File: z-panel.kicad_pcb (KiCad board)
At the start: 2 copper layers, 80 x 80 mm, 27 parts, among them J1 MOLEX_FFC-14, J2 PC104PTH, J3 PC104PTH, J4 PC104PTH, J5 PC104PTH, J6 SMA, U100 OPA380, U110 OPA380, U120 OPA380, U130 OPA380

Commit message: added 3d model for photodiode
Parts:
- moved D100 4.47 mm to (200.0, 111.0)
- moved D110 3.16 mm to (216.0, 110.0)
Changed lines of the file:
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@@
   (general
     (links 62)
-    (no_connects 22)
+    (no_connects 61)
     (area 109.924999 59.924999 190.075001 140.075001)
     (thickness 1.6)
-    (drawings 4)
+    (drawings 8)
     (tracks 0)
     (zones 0)
@@
   )
   (module SFUSat:SFH2430 (layer F.Cu)
-    (at 204 109)
+    (at 200 111)
     (fp_text reference D100 (at 1.5 3.25) (layer F.SilkS)
       (effects (font (size 1 1) (thickness 0.15)))
@@
     (pad 1 smd rect (at 3.05 0) (size 1.4 2) (layers F.Cu F.Paste F.Mask)
       (net 3 "Net-(C100-Pad2)"))
+    (model ../../../../../home/tobi/Cubesat/z-panel/KiCad-Lib/SFUSat.pretty/SFH_2430.wrl
+      (at (xyz 0 0 0))
+      (scale (xyz 1 1 1))
+      (rotate (xyz 0 0 0))
+    )
   )
   (module SFUSat:SFH2430 (layer F.Cu)
-    (at 213 109)
+    (at 216 110)
     (fp_text reference D110 (at 1.5 3.25) (layer F.SilkS)
       (effects (font (size 1 1) (thickness 0.15)))
@@
     (pad 1 smd rect (at 3.05 0) (size 1.4 2) (layers F.Cu F.Paste F.Mask)
       (net 5 "Net-(C110-Pad2)"))
+    (model ../../../../../home/tobi/Cubesat/z-panel/KiCad-Lib/SFUSat.pretty/SFH_2430.wrl
+      (at (xyz 0 0 0))
+      (scale (xyz 1 1 1))
+      (rotate (xyz 0 0 0))
+    )
   )
   (module SFUSat:SFH2430 (layer F.Cu)
@@
     (pad 1 smd rect (at 3.05 0) (size 1.4 2) (layers F.Cu F.Paste F.Mask)
       (net 7 "Net-(C120-Pad2)"))
+    (model ../../../../../home/tobi/Cubesat/z-panel/KiCad-Lib/SFUSat.pretty/SFH_2430.wrl
+      (at (xyz 0 0 0))
+      (scale (xyz 1 1 1))
+      (rotate (xyz 0 0 0))
+    )
   )
   (module SFUSat:SFH2430 (layer F.Cu)
@@
     (pad 1 smd rect (at 3.05 0) (size 1.4 2) (layers F.Cu F.Paste F.Mask)
       (net 9 "Net-(C130-Pad2)"))
+    (model ../../../../../home/tobi/Cubesat/z-panel/KiCad-Lib/SFUSat.pretty/SFH_2430.wrl
+      (at (xyz 0 0 0))
+      (scale (xyz 1 1 1))
+      (rotate (xyz 0 0 0))
+    )
   )
   (module SFUSat:MOLEX_FFC-14 (layer F.Cu)
@@
   (module SFUSat:VSSOP_8 (layer F.Cu)
     (at 214 73)
-    (fp_text reference U130 (at -0.1 4.1) (layer F.SilkS)
+    (fp_text reference U130 (at 3 -1) (layer F.SilkS)
       (effects (font (size 1 1) (thickness 0.15)))
     )
@@
       (solder_paste_margin_ratio -0.1))
   )
+  (dimension 4 (width 0.3) (layer Dwgs.User)
+    (gr_text "4.000 mm" (at 103.65 62 270) (layer Dwgs.User)
+      (effects (font (size 1.5 1.5) (thickness 0.3)))
+    )
+    (feature1 (pts (xy 114 64) (xy 102.3 64)))
+    (feature2 (pts (xy 114 60) (xy 102.3 60)))
+    (crossbar (pts (xy 105 60) (xy 105 64)))
+    (arrow1a (pts (xy 105 64) (xy 104.413579 62.873496)))
+    (arrow1b (pts (xy 105 64) (xy 105.586421 62.873496)))
+    (arrow2a (pts (xy 105 60) (xy 104.413579 61.126504)))
+    (arrow2b (pts (xy 105 60) (xy 105.586421 61.126504)))
+  )
+  (dimension 4 (width 0.3) (layer Dwgs.User)
+    (gr_text "4.000 mm" (at 112 55.65) (layer Dwgs.User)
+      (effects (font (size 1.5 1.5) (thickness 0.3)))
+    )
+    (feature1 (pts (xy 110 64) (xy 110 54.3)))
+    (feature2 (pts (xy 114 64) (xy 114 54.3)))
+    (crossbar (pts (xy 114 57) (xy 110 57)))
+    (arrow1a (pts (xy 110 57) (xy 111.126504 56.413579)))
+    (arrow1b (pts (xy 110 57) (xy 111.126504 57.586421)))
+    (arrow2a (pts (xy 114 57) (xy 112.873496 56.413579)))
+    (arrow2b (pts (xy 114 57) (xy 112.873496 57.586421)))
+  )
+  (dimension 80 (width 0.3) (layer Dwgs.User)
+    (gr_text "80.000 mm" (at 150 49.65) (layer Dwgs.User)
+      (effects (font (size 1.5 1.5) (thickness 0.3)))
+    )
+    (feature1 (pts (xy 190 60) (xy 190 48.3)))
+    (feature2 (pts (xy 110 60) (xy 110 48.3)))
+    (crossbar (pts (xy 110 51) (xy 190 51)))
+    (arrow1a (pts (xy 190 51) (xy 188.873496 51.586421)))
+    (arrow1b (pts (xy 190 51) (xy 188.873496 50.413579)))
+    (arrow2a (pts (xy 110 51) (xy 111.126504 51.586421)))
+    (arrow2b (pts (xy 110 51) (xy 111.126504 50.413579)))
+  )
+  (dimension 80 (width 0.3) (layer Dwgs.User)
+    (gr_text "80.000 mm" (at 96.65 100 270) (layer Dwgs.User)
+      (effects (font (size 1.5 1.5) (thickness 0.3)))
+    )
+    (feature1 (pts (xy 110 140) (xy 95.3 140)))
+    (feature2 (pts (xy 110 60) (xy 95.3 60)))
+    (crossbar (pts (xy 98 60) (xy 98 140)))
+    (arrow1a (pts (xy 98 140) (xy 97.413579 138.873496)))
+    (arrow1b (pts (xy 98 140) (xy 98.586421 138.873496)))
+    (arrow2a (pts (xy 98 60) (xy 97.413579 61.126504)))
+    (arrow2b (pts (xy 98 60) (xy 98.586421 61.126504)))
+  )
   (gr_line (start 190 60) (end 190 140) (layer Edge.Cuts) (width 0.15))

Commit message: layout complete
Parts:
- added REF**: FFC-Fasteners-8mm, SFUSat:FFC-Fasteners-8mm, F.Cu at (150.0, 134.0)
- moved D130 110.9 mm to (114.2, 125.4), turned to 90 degrees
- moved U130 107.8 mm to (119.8, 125.4), turned to 270 degrees
- moved R130 99.8 mm to (119.8, 120.8), turned to 180 degrees
- moved R131 99.6 mm to (123.8, 126.2), turned to 270 degrees
- moved C130 99.1 mm to (119.8, 122.2), turned to 180 degrees
- moved D100 93.0 mm to (114.2, 75.0), turned to 90 degrees
- moved U100 91.8 mm to (120.0, 75.0), turned to 270 degrees
- moved C100 89.7 mm to (120.0, 72.0), turned to 180 degrees
- moved R100 89.1 mm to (120.0, 70.6), turned to 180 degrees
- moved R101 86.9 mm to (124.0, 75.8), turned to 270 degrees
- moved U120 56.8 mm to (180.4, 125.2), turned to 90 degrees
- moved R121 52.0 mm to (176.4, 124.4), turned to 90 degrees
- moved R120 51.8 mm to (180.4, 129.6)
- moved D120 51.7 mm to (186.2, 125.2), turned to 270 degrees
- moved U110 49.6 mm to (180.0, 75.0), turned to 90 degrees
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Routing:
- net /3V3: track 0.00 -> 171.5 mm, vias 0 -> 6
- net /D2: track 0.00 -> 127.5 mm
- net /D1: track 0.00 -> 79.9 mm
- net /D4: track 0.00 -> 37.0 mm
- net /D3: track 0.00 -> 36.7 mm
- net GND: track 0.00 -> 29.3 mm, vias 0 -> 20
- net Net-(A1-Pad1): track 0.00 -> 29.0 mm
- net Net-(C110-Pad2): track 0.00 -> 10.6 mm
- net Net-(C130-Pad2): track 0.00 -> 10.6 mm
- net Net-(C100-Pad2): track 0.00 -> 10.6 mm
- net Net-(C120-Pad2): track 0.00 -> 10.6 mm
- added copper zone on B.Cu, net GND
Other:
- outline, holes or cut-outs redrawn
- net class Long added: clearance 0.2, trace_width 0.25, via_dia 0.6, via_drill 0.4
- net class RF added: clearance 0.2, trace_width 1.11538, via_dia 0.6, via_drill 0.4

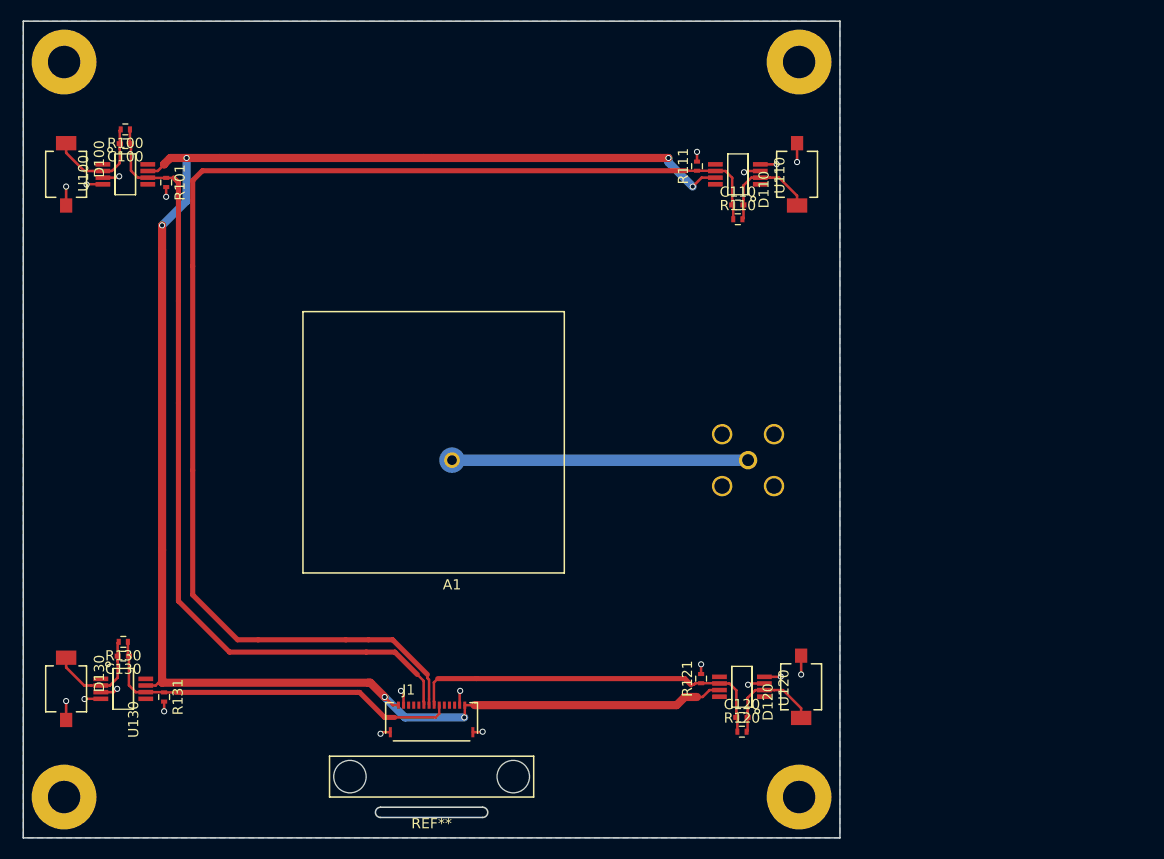
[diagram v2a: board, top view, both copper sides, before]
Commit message: added slots for coax access and adjusted FFC position
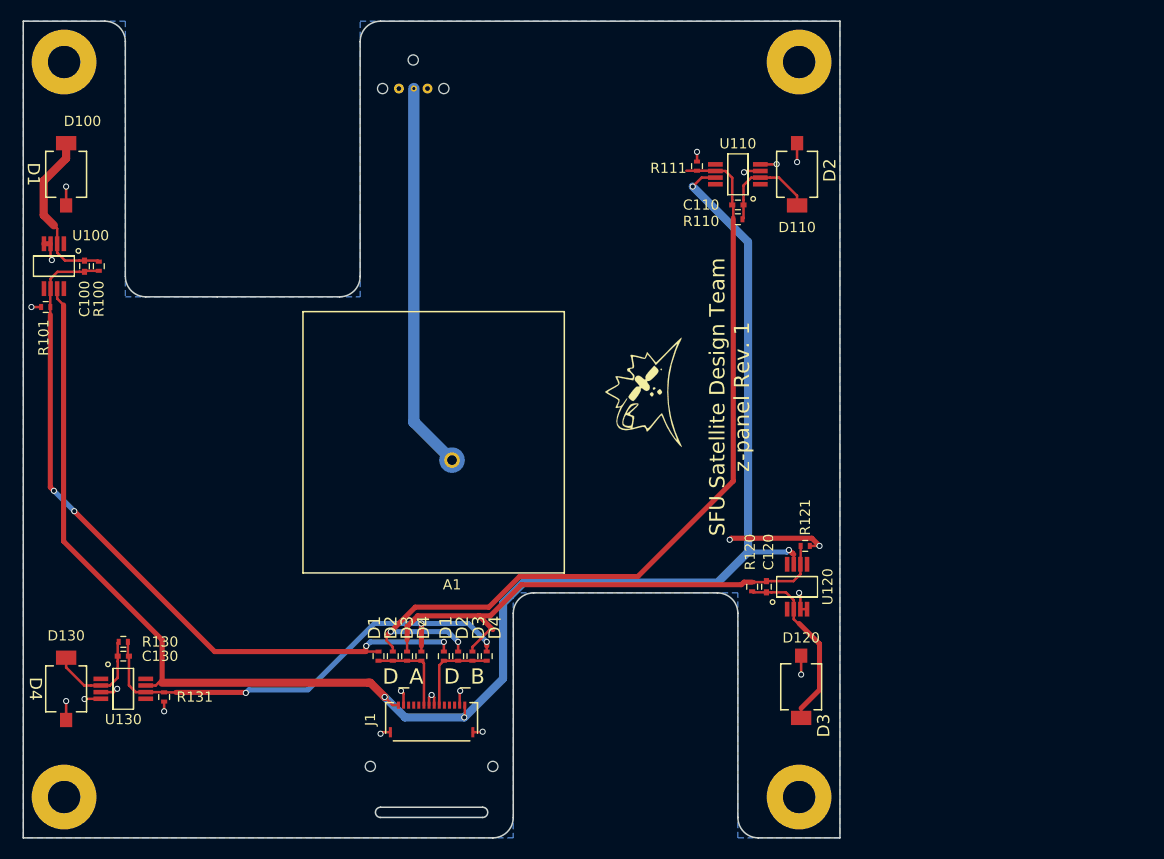
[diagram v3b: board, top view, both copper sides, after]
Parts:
- removed the REF** at (150.0, 134.0)
- added G***: LOGO, SFUSat:SFUSat_15mm_2, F.Cu at (170.8, 96.4)
- added J7: TEST_1P, SFUSat:via-0.97mm, F.Cu at (149.6, 66.6)
- added J8: TEST_1P, SFUSat:via-0.97mm, F.Cu at (146.8, 66.6)
- added R1: 0R, SFUSat-res:R_0402, F.Cu at (144.8, 122.2)
- added R2: 0R, SFUSat-res:R_0402, F.Cu at (151.2, 122.2)
- added R3: 0R, SFUSat-res:R_0402, F.Cu at (146.2, 122.2)
- added R4: 0R, SFUSat-res:R_0402, F.Cu at (152.6, 122.2)
- added R5: 0R, SFUSat-res:R_0402, F.Cu at (147.6, 122.2)
- added R6: 0R, SFUSat-res:R_0402, F.Cu at (154.0, 122.2)
- added R7: 0R, SFUSat-res:R_0402, F.Cu at (149.0, 122.2)
- added R8: 0R, SFUSat-res:R_0402, F.Cu at (155.4, 122.2)
- added REF**: NPTH-1mm, SFUSat:NPTH-1mm, F.Cu at (148.2, 63.8)
- added REF**: NPTH-1mm, SFUSat:NPTH-1mm, F.Cu at (151.2, 66.6)
- added REF**: NPTH-1mm, SFUSat:NPTH-1mm, F.Cu at (156.0, 133.0)
- added REF**: NPTH-1mm, SFUSat:NPTH-1mm, F.Cu at (144.0, 133.0)
- added REF**: NPTH-1mm, SFUSat:NPTH-1mm, F.Cu at (145.2, 66.6)
- J6: value SMA -> TEST_1P; footprint SFUSat:MCX -> SFUSat:vis-0.6mm
- moved J6 47.0 mm to (152.0, 66.0)
- moved R101 17.0 mm to (112.2, 88.0), turned to 180 degrees
- moved R121 16.5 mm to (186.6, 111.4), turned to 0 degrees
- moved R120 14.2 mm to (181.4, 115.4), turned to 270 degrees
- moved R100 13.6 mm to (117.4, 84.0), turned to 90 degrees
- moved C120 13.0 mm to (182.8, 115.4), turned to 270 degrees
- moved C100 12.6 mm to (116.0, 84.0), turned to 90 degrees
- moved U100 11.4 mm to (113.0, 84.0), turned to 180 degrees
- moved U120 11.2 mm to (185.8, 115.4), turned to 0 degrees
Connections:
- J1 pad 6: /D1 -> /D_A
- J1 pad 7: /D2 -> GND
- J1 pad 8: /D3 -> GND
- J1 pad 9: /D4 -> /D_B
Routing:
- net /D2: track 127.5 -> 84.5 mm, vias 0 -> 2
- net /D3: track 36.7 -> 51.0 mm
- net /D4: track 37.0 -> 46.9 mm, vias 0 -> 3
- net GND: track 29.3 -> 38.7 mm
- net Net-(A1-Pad1): track 29.0 -> 37.9 mm
- net /D_B: track 0.00 -> 8.74 mm
- net /D_A: track 0.00 -> 8.65 mm
- net /3V3: track 171.5 -> 163.7 mm, vias 6 -> 4
- net Net-(C120-Pad2): track 10.6 -> 17.8 mm
- net /D1: track 79.9 -> 73.6 mm, vias 0 -> 4
- net Net-(C100-Pad2): track 10.6 -> 16.6 mm
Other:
- outline, holes or cut-outs redrawn
- rule pad_to_mask_clearance: 0.2 -> 0.03
- board text added: "+Y"
- board text added: "+x"
- board text added: "-Y"
- board text added: "-x"
- board text added: "D1"
- board text added: "D2"
- board text added: "D3"
- board text added: "D4"
- board text added: "D_A"
- board text added: "D_B"
- board text added: "GPS Coax"
- board text added: "SFU Satellite Design Team z-panel Rev. 1"
